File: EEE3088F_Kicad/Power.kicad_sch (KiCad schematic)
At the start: 15 parts, among them Q1 CJ2301 S1, U1 MCP73831T-2ACI/OT, U2 L78L33ACUTR

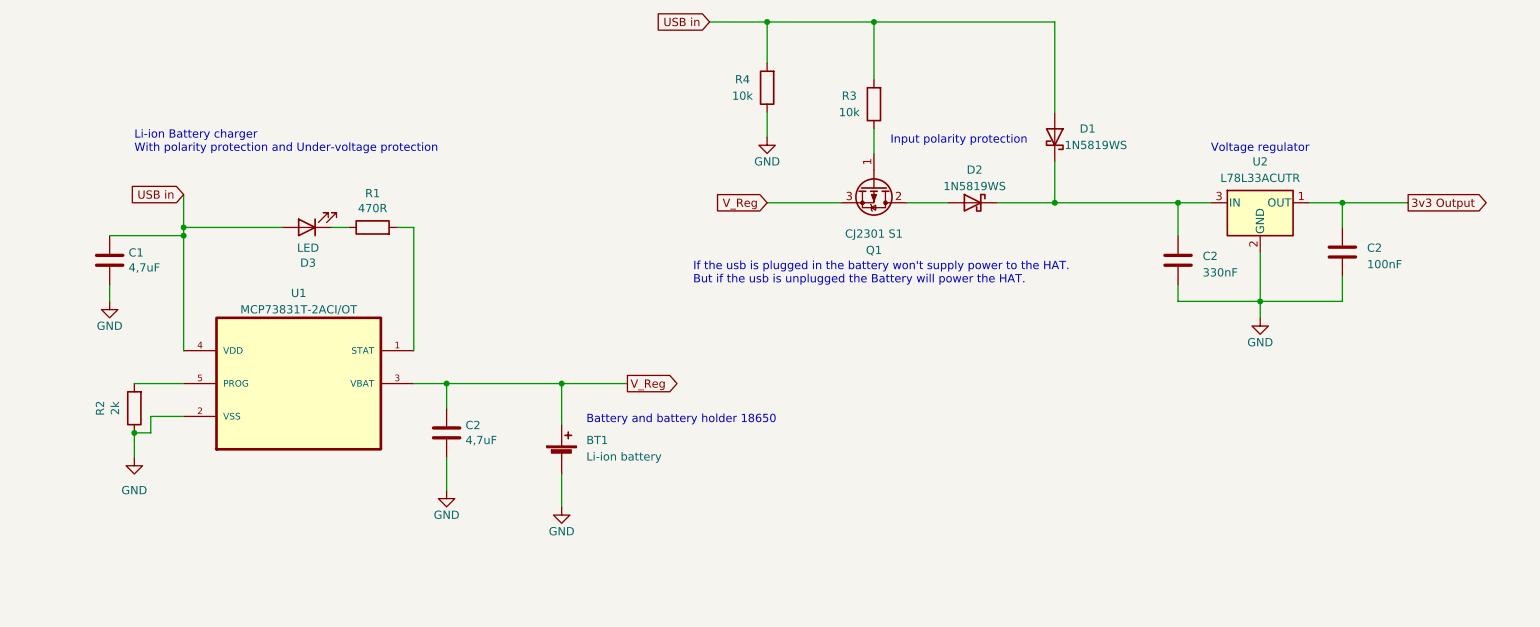
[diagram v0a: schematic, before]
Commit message: I updated my power schematic
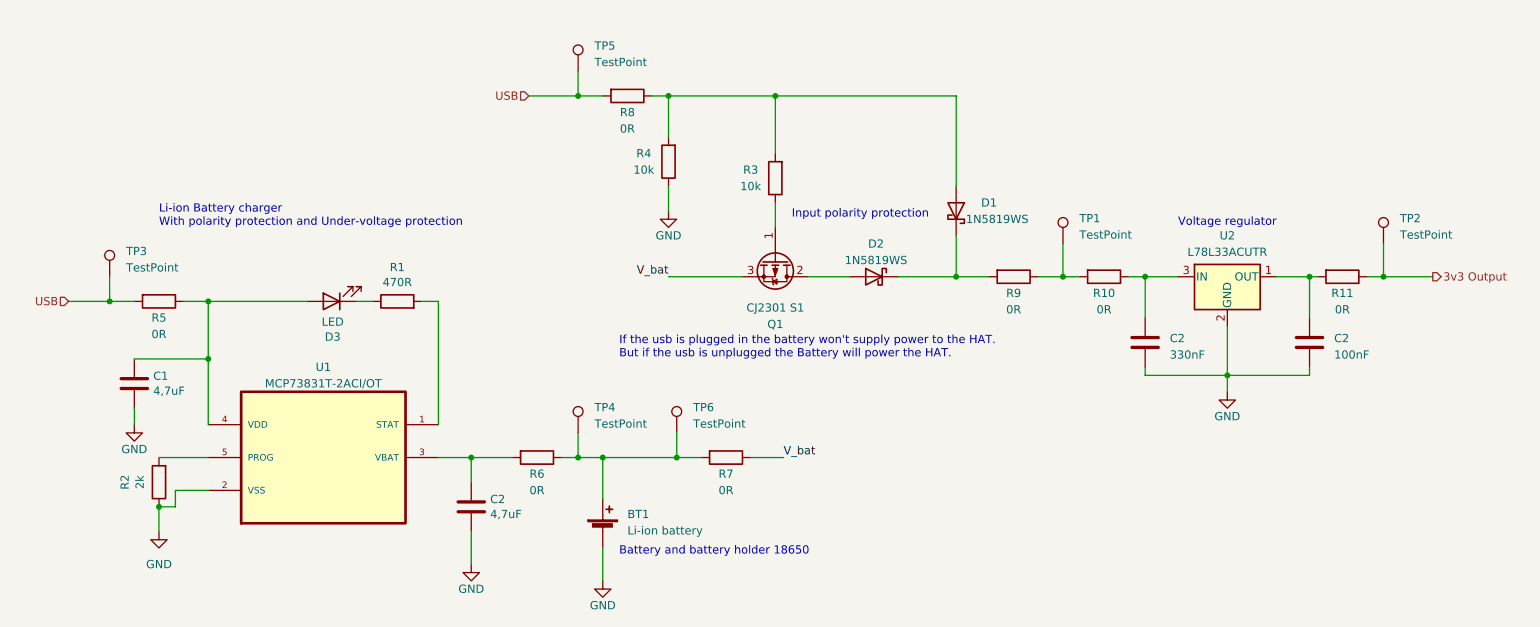
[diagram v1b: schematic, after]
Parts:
- removed C2: 100nF, EEE3088F_Footprints:CAPC3216X180N, symbol Device:C
- removed C2: 4,7uF, symbol Device:C
- removed C2: 330nF, EEE3088F_Footprints:CAPC3216X180N, symbol Device:C
- added C2: 4,7uF, symbol Device:C
- added C2: 330nF, EEE3088F_Footprints:CAPC3216X180N, symbol Device:C
- added C2: 100nF, EEE3088F_Footprints:CAPC3216X180N, symbol Device:C
- added R10, R11, R5, R6, R7, R8, R9: 0R, symbol Device:R
- added TP1, TP2, TP3, TP4, TP5, TP6: TestPoint, symbol Connector:TestPoint
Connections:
- net 3v3 Output: now also R11.1, TP2.1; no longer U2.1 (OUT)
- net GND: now also C2.2, C2.2, C2.2
- net at D1.1 (K), D2.1 (K): now also R9.2; no longer U2.3 (IN)
- net USB in: no longer names the net of D1.2 (A), R3.2, R4.2
- net USB in: now also R8.1; no longer C1.1, D3.2 (A), U1.4 (VDD)
- removed net V_Reg: BT1.1 (+), Q1.3 (S), U1.3 (VBAT)
- new net: C2.1, R6.2, U1.3 (VBAT)
- new net: BT1.1 (+), R6.1, R7.2, TP4.1, TP6.1
- new net: C2.1, R11.2, U2.1 (OUT)
- new net: C2.1, R10.1, U2.3 (IN)
- new net: C1.1, D3.2 (A), R5.1, U1.4 (VDD)
- new net: R10.2, R9.1, TP1.1
- new net USB: R5.2, R8.2, TP3.1, TP5.1
- new net V_bat: Q1.3 (S), R7.1
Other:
- company: (none) -> UCT
- title: (none) -> Power Subsystem

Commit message: added LCSC numbers to components
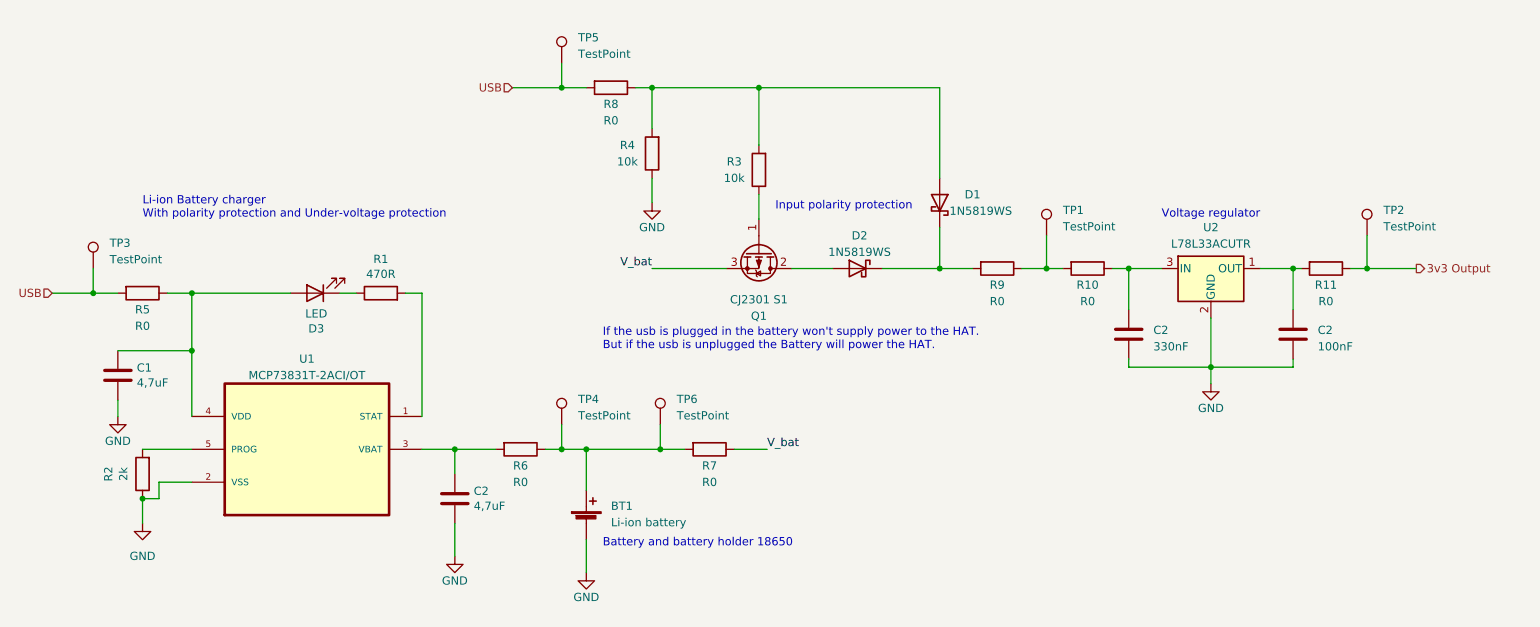
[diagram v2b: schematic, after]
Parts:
- removed C2: 4,7uF, symbol Device:C
- removed C2: 330nF, EEE3088F_Footprints:CAPC3216X180N, symbol Device:C
- removed C2: 100nF, EEE3088F_Footprints:CAPC3216X180N, symbol Device:C
- added C2: 330nF, EEE3088F_Footprints:CAPC3216X180N, symbol Device:C
- added C2: 4,7uF, symbol Device:C
- added C2: 100nF, EEE3088F_Footprints:CAPC3216X180N, symbol Device:C
- C1: JLCPCB Part C8032 -> (none); LCSC (none) -> C1779
- D1, D2: LCSC (none) -> C191023
- D3: JLCPCB Part C264544 -> (none); LCSC (none) -> C2286
- R1: LCSC (none) -> C17710
- R10, R11, R5, R6, R7, R8, R9: value 0R -> R0; LCSC (none) -> C17888
- R2: LCSC (none) -> C17944
- R3, R4: LCSC (none) -> C17902
- U1: JLCPCB C424093 -> (none); LCSC (none) -> C424093
- U2: LCSC (none) -> C14170
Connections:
- net GND: now also C2.2, C2.2, C2.2
- net at R6.2, U1.3 (VBAT): now also C2.1
- net at R11.2, U2.1 (OUT): now also C2.1
- net at R10.1, U2.3 (IN): now also C2.1
